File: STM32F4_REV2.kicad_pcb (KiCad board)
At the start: 4 copper layers, 56 x 51 mm, 54 parts, among them J1 Screw_Terminal_01x02, J2 SWD, J3 Conn_01x04, J4 Conn_01x04, J5 USB_B_Micro, Q1 AO3401A, SW1 SW_SPDT, U1 MP2359DJ-LF-Z, U2 STM32F405RGT6, U3 USBLC6-2SC6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

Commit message: Updated the schematics and PCB
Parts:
- removed G***: LOGO, SchmillipKiCADLibrary:Silk_PhilsLabIC
- removed J3, J4: Conn_01x04, Connector_Molex:Molex_PicoBlade_53048-0410_1x04_P1.25mm_Horizontal
- removed Q1: AO3401A, Package_TO_SOT_SMD:SOT-23
- J1: value Screw_Terminal_01x02 -> Conn_01x22; footprint TerminalBlock_Phoenix:TerminalBlock_Phoenix_PT-1,5-2-3.5-H_1x02_P3.50mm_Horizontal -> Connector_PinHeader_2.54mm:PinHeader_1x22_P2.54mm_Horizontal
- moved H2 58.8 mm to (140.0, 80.5)
- moved H1 58.5 mm to (139.8, 41.0)
- moved J1 22.6 mm to (100.2, 82.8), turned to 270 degrees
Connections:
- J1 pad 1: +12V -> Net-(J1-Pad1)
- J1 pad 2: GND -> Net-(J1-Pad2)
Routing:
- net +12V: track 8.72 -> 0.00 mm
- net USART3_TX: track 14.0 -> 6.02 mm
- net USART3_RX: track 13.7 -> 6.21 mm
- net Net-(D1-Pad1): track 4.80 -> 2.20 mm
- net GND: track 65.9 -> 64.1 mm, vias 42 -> 40
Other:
- board size 56 x 51 mm -> 114.8 x 51 mm
- board text removed: "STM32F4 TEST BOARD | REV 2"
- board text removed: "UART"

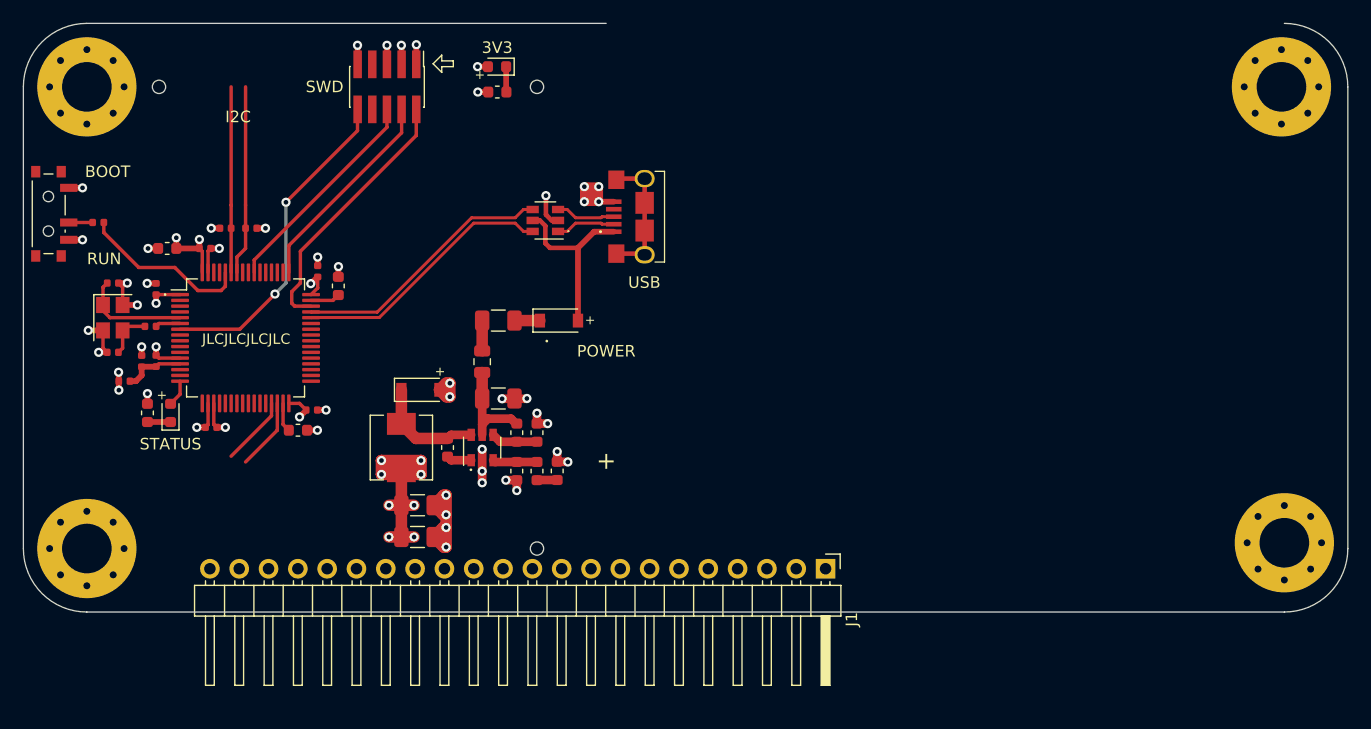
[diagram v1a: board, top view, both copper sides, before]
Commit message: Added some datasheets for thermocouple and updated schematics and PCB
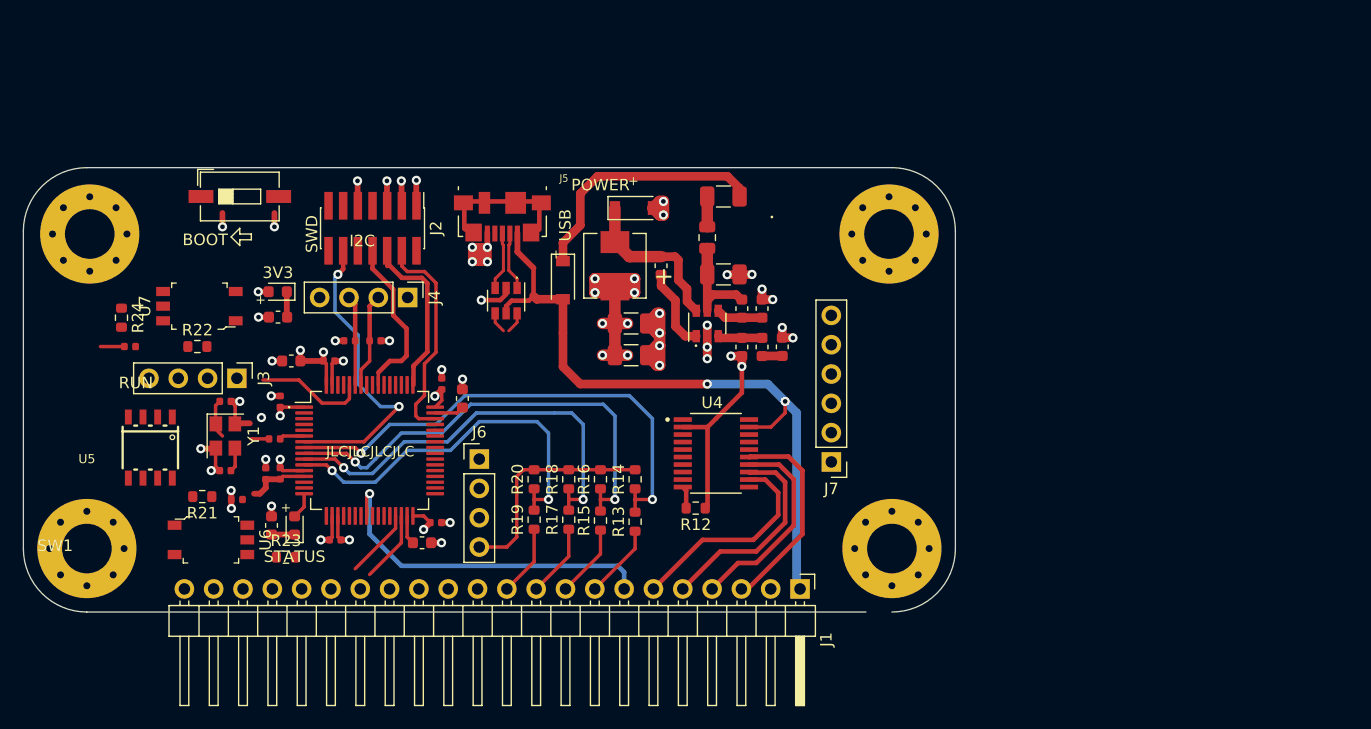
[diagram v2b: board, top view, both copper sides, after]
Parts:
- removed REF** (x3): MountingHole_1.152mm, SchmillipKiCADLibrary:JLCPCB_MountingHole_1.152mm
- added J3: Conn_01x04, Connector_PinHeader_2.54mm:PinHeader_1x04_P2.54mm_Vertical, F.Cu at (49.2, 66.2)
- added J4: Conn_01x04, Connector_PinHeader_2.54mm:PinHeader_1x04_P2.54mm_Vertical, F.Cu at (64.0, 59.2)
- added J6: Conn_01x04, Connector_PinHeader_2.54mm:PinHeader_1x04_P2.54mm_Vertical, F.Cu at (70.2, 73.2)
- added J7: Conn_01x06, Connector_PinHeader_2.54mm:PinHeader_1x06_P2.54mm_Vertical, F.Cu at (100.8, 73.5)
- added R12: 15k, Resistor_SMD:R_0603_1608Metric, F.Cu at (89.0, 77.5)
- added R13: 10k, Resistor_SMD:R_0603_1608Metric, F.Cu at (83.8, 78.7)
- added R14: 15k, Resistor_SMD:R_0603_1608Metric, F.Cu at (83.8, 75.0)
- added R15: 10k, Resistor_SMD:R_0603_1608Metric, F.Cu at (80.8, 78.6)
- added R16: 15k, Resistor_SMD:R_0603_1608Metric, F.Cu at (80.8, 75.0)
- added R17: 10k, Resistor_SMD:R_0603_1608Metric, F.Cu at (78.0, 78.5)
- added R18: 15k, Resistor_SMD:R_0603_1608Metric, F.Cu at (78.0, 75.0)
- added R19: 10k, Resistor_SMD:R_0603_1608Metric, F.Cu at (75.0, 78.5)
- added R20: 15k, Resistor_SMD:R_0603_1608Metric, F.Cu at (75.0, 75.0)
- added R21: 1.5k, Resistor_SMD:R_0603_1608Metric, F.Cu at (46.2, 76.5)
- added R22: 1k, Resistor_SMD:R_0603_1608Metric, F.Cu at (45.8, 63.5)
- added R23: 10k, Resistor_SMD:R_0603_1608Metric, F.Cu at (53.5, 81.8)
- added R24: 10k, Resistor_SMD:R_0603_1608Metric, F.Cu at (39.2, 61.0)
- added U4: TXS0108EPWR, robot_regulator:SOP65P640X120-20N, F.Cu at (90.8, 72.8)
- added U5: TJA1051T, robot_regulator:SOT96-1, F.Cu at (41.8, 72.2)
- added U6: TLP2361, TLP2361:SOIC-6-5_W4.55mm, F.Cu at (47.0, 80.2)
- added U7: TLP2361, TLP2361:SOIC-6-5_W4.55mm, F.Cu at (46.0, 60.0)
- J2: value SWD -> Conn_ST_STDC14; footprint Connector_PinHeader_1.27mm:PinHeader_2x05_P1.27mm_Vertical_SMD -> Connector_PinHeader_1.27mm:PinHeader_2x07_P1.27mm_Vertical_SMD
- J5: footprint SchmillipKiCADLibrary:USB_MICRO_B_101181930001LF -> USB_Micro-B_Molex_47346-0001:USB_Micro-B_Molex_47346-0001
- SW1: value SW_SPDT -> SW_DIP_x01; footprint Button_Switch_SMD:SW_SPDT_PCM12 -> Button_Switch_SMD:SW_DIP_SPSTx01_Slide_6.7x4.1mm_W6.73mm_P2.54mm_LowProfile_JPin
- Y1: footprint Crystal:Crystal_SMD_3225-4Pin_3.2x2.5mm -> Oscillator:Oscillator_SMD_Abracon_ASE-4Pin_3.2x2.5mm
- moved H1 36.3 mm to (105.8, 53.8)
- moved H2 34.0 mm to (106.0, 81.0)
- moved R6 27.2 mm to (52.8, 61.0)
- moved D3 27.2 mm to (52.8, 58.8)
- moved C2 24.3 mm to (83.4, 61.5)
- moved C3 24.3 mm to (83.4, 64.2)
- moved C4 24.3 mm to (86.0, 56.5)
- moved D2 24.3 mm to (83.7, 51.5)
- moved L1 24.3 mm to (82.0, 56.5)
- moved R1 22.3 mm to (93.0, 60.2)
- moved R2 22.3 mm to (94.8, 60.2)
- moved R5 22.3 mm to (96.5, 63.5)
- moved C1 22.3 mm to (91.4, 57.2)
- moved F1 22.3 mm to (91.4, 50.5)
- moved FB1 22.3 mm to (90.0, 54.1)
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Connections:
- J1 pad 1: Net-(J1-Pad1) -> +5V
- J1 pad 10: Net-(J1-Pad10) -> A2_5
- J1 pad 11: Net-(J1-Pad11) -> A3_5
- J1 pad 12: Net-(J1-Pad12) -> INT
- J1 pad 13: Net-(J1-Pad13) -> CS
- J1 pad 14: Net-(J1-Pad14) -> SCK
- J1 pad 15: Net-(J1-Pad15) -> MOSI
- J1 pad 16: Net-(J1-Pad16) -> MISO
- J1 pad 17: Net-(J1-Pad17) -> COUT1
- J1 pad 18: Net-(J1-Pad18) -> COUT2
- J1 pad 19: Net-(J1-Pad19) -> ISO_5V
- J1 pad 2: Net-(J1-Pad2) -> GND
- J1 pad 20: Net-(J1-Pad20) -> ISO_GND
- J1 pad 21: Net-(J1-Pad21) -> CANH
- J1 pad 22: Net-(J1-Pad22) -> CANL
- J1 pad 3: Net-(J1-Pad3) -> B5
- J1 pad 4: Net-(J1-Pad4) -> B6
- J1 pad 5: Net-(J1-Pad5) -> B7
- J1 pad 6: Net-(J1-Pad6) -> B8
- J1 pad 7: Net-(J1-Pad7) -> DAC
- J1 pad 8: Net-(J1-Pad8) -> A0_5
- J1 pad 9: Net-(J1-Pad9) -> A1_5
- J2 pad 1: +3V3 -> Net-(J2-Pad1)
- J2 pad 10: NRST -> Net-(J2-Pad10)
- J2 pad 2: SWDIO -> Net-(J2-Pad2)
- J2 pad 3: GND -> +3V3
- J2 pad 4: SWCLK -> SWDIO
- J2 pad 6: SWO -> SWCLK
- J2 pad 7: Net-(J2-Pad7) -> GND
- J2 pad 8: Net-(J2-Pad8) -> SWO
- J2 pad 9: GND -> Net-(J2-Pad9)
- R7 pad 1: Net-(R7-Pad1) -> +3V3
- SW1 pad 1: +3V3 -> BOOT0
- SW1 pad 2: Net-(R7-Pad1) -> GND
- U2 pad 10: Net-(U2-Pad10) -> A2
- U2 pad 11: Net-(U2-Pad11) -> A3
- U2 pad 14: Net-(U2-Pad14) -> THERMOCOUPLE_CS
- U2 pad 24: Net-(U2-Pad24) -> DAC
- U2 pad 26: Net-(U2-Pad26) -> ENABLEDISABLE
- U2 pad 33: Net-(U2-Pad33) -> CS
- U2 pad 34: Net-(U2-Pad34) -> SCK
- U2 pad 35: Net-(U2-Pad35) -> MISO
- U2 pad 36: Net-(U2-Pad36) -> MOSI
- U2 pad 37: Net-(U2-Pad37) -> INT
- U2 pad 38: Net-(U2-Pad38) -> COUT1
- U2 pad 39: Net-(U2-Pad39) -> COUT2
- U2 pad 61: Net-(U2-Pad61) -> CAN_RX
- U2 pad 62: Net-(U2-Pad62) -> CAN_TX
- U2 pad 8: Net-(U2-Pad8) -> A0
- U2 pad 9: Net-(U2-Pad9) -> A1
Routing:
- net +5V: track 15.8 -> 59.9 mm, vias 0 -> 2
- net A0: track 0.00 -> 43.8 mm, vias 0 -> 2
- net A1: track 0.00 -> 40.6 mm, vias 0 -> 2
- net A2: track 0.00 -> 36.9 mm, vias 0 -> 2
- net A3: track 0.00 -> 33.2 mm, vias 0 -> 2
- net DAC: track 0.00 -> 30.4 mm, vias 0 -> 1
- net USB_D-: track 22.9 -> 1.84 mm
- net USB_D+: track 22.9 -> 1.84 mm
- net Net-(D1-Pad1): track 2.20 -> 22.0 mm
- net B8: track 0.00 -> 18.4 mm
- net B7: track 0.00 -> 18.2 mm
- net B5: track 0.00 -> 17.9 mm
- net B6: track 0.00 -> 17.8 mm
- net +3V3: track 52.7 -> 70.4 mm
- net GND: track 64.1 -> 80.1 mm, vias 40 -> 38
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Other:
- board size 114.8 x 51 mm -> 80.8 x 38.5 mm
